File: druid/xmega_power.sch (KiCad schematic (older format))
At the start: 32 parts, among them P9 CONN_01X02, U4 XC6206P332MR

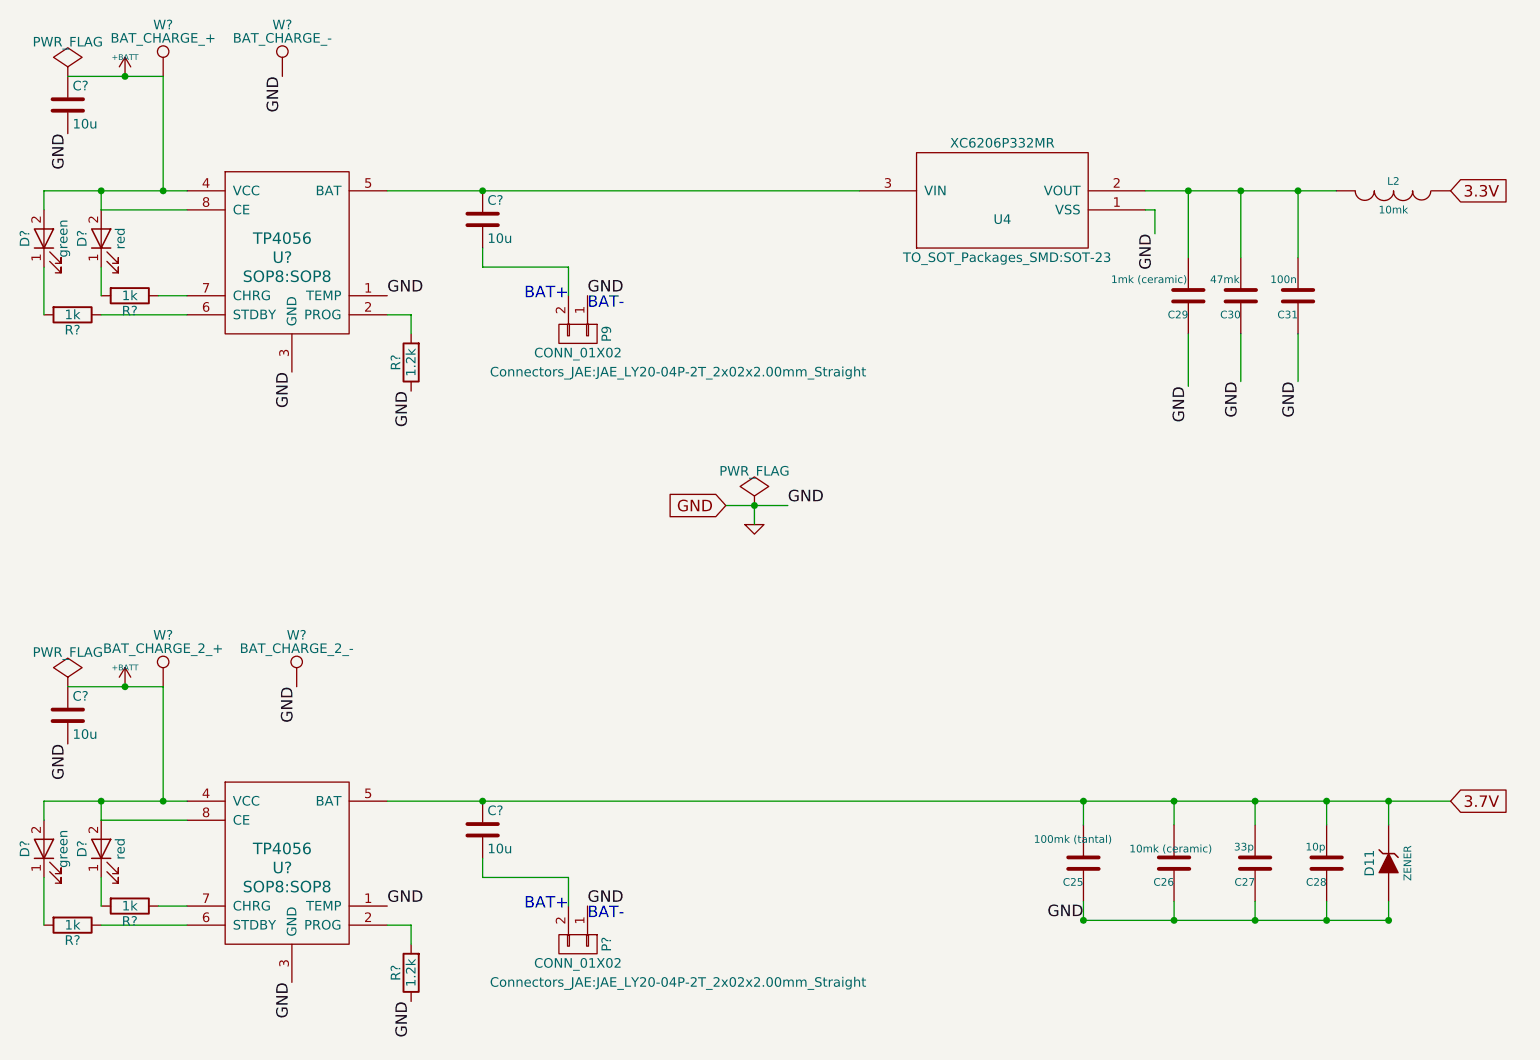
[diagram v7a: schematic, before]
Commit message: Bat connectors replaced by test points
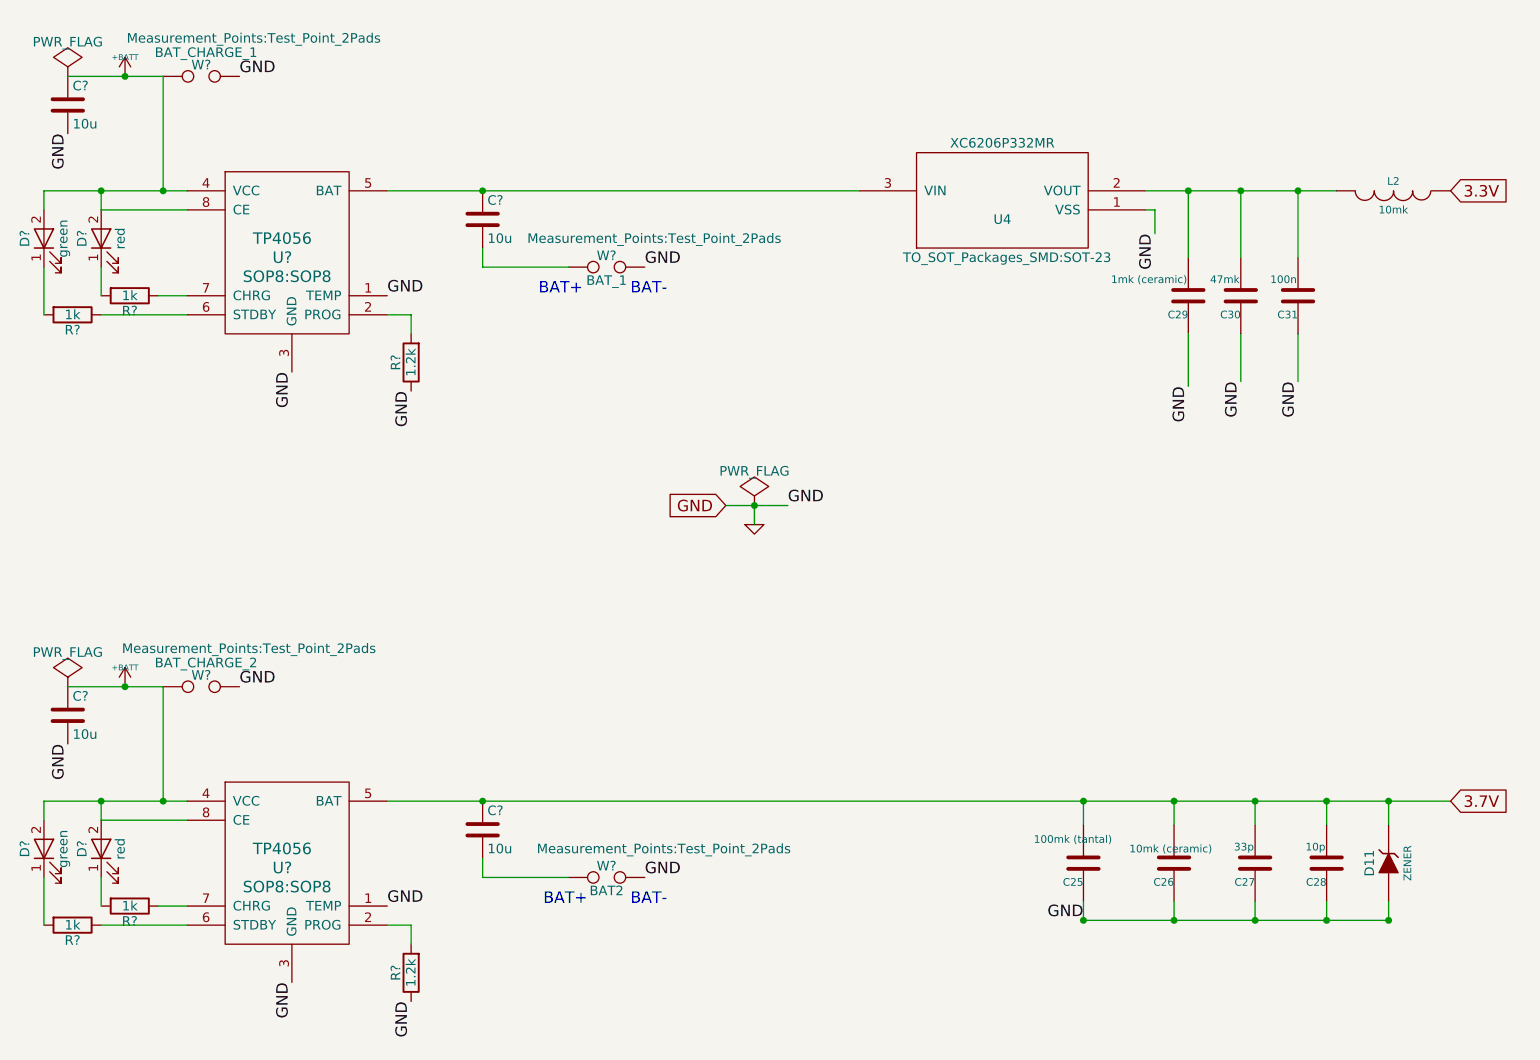
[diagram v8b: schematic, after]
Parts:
- removed P9, P?: CONN_01X02, Connectors_JAE:JAE_LY20-04P-2T_2x02x2.00mm_Straight, symbol CONN_01X02
- removed W?: BAT_CHARGE_+, symbol TEST_1P
- removed W?: BAT_CHARGE_-, symbol TEST_1P
- removed W?: BAT_CHARGE_2_+, symbol TEST_1P
- removed W?: BAT_CHARGE_2_-, symbol TEST_1P
- added W?: BAT_1, Measurement_Points:Test_Point_2Pads, symbol TEST
- added W?: BAT2, Measurement_Points:Test_Point_2Pads, symbol TEST
- added W?: BAT_CHARGE_1, Measurement_Points:Test_Point_2Pads, symbol TEST
- added W?: BAT_CHARGE_2, Measurement_Points:Test_Point_2Pads, symbol TEST
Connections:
- net +BATT: now also W?.1, W?.1
- net GND: now also W?.2, W?.2, W?.2, W?.2
- net at C?.2: now also W?.1 (x2)
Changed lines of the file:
@@
 Wire Wire Line
 	3825 2050 6300 2050
-$Comp
-L CONN_01X02 P9
-U 1 1 5AB7EB32
-P 4825 2800
-F 0 "P9" H 4825 2950 50  0000 C CNN
-F 1 "CONN_01X02" V 4925 2800 50  0000 C CNN
-F 2 "Connectors_JAE:JAE_LY20-04P-2T_2x02x2.00mm_Straight" V 5025 3325 50  0000 C CNN
-F 3 "" H 4825 2800 50  0000 C CNN
-	1    4825 2800
-	0    1    1    0
-$EndComp
 Text GLabel 5600 3700 0    60   Input ~ 0
 GND
@@
 Wire Wire Line
 	4325 2450 4775 2450
-Wire Wire Line
-	4775 2450 4775 2600
-Text Label 4875 2600 0    60   ~ 0
-GND
-Text Notes 4875 2675 0    60   ~ 0
+Text Label 5175 2450 0    60   ~ 0
+GND
+Text Notes 5100 2600 0    60   ~ 0
 BAT-
-Text Notes 4775 2625 2    60   ~ 0
+Text Notes 4850 2600 2    60   ~ 0
 BAT+\n
 $Comp
@@
 Text Label 3325 3000 3    60   ~ 0
 GND
-$Comp
-L TEST_1P W?
-U 1 1 5C6AC0DE
-P 2650 1450
-F 0 "W?" H 2650 1720 50  0000 C CNN
-F 1 "BAT_CHARGE_+" H 2650 1650 50  0000 C CNN
-F 2 "" H 2850 1450 50  0000 C CNN
-F 3 "" H 2850 1450 50  0000 C CNN
-	1    2650 1450
-	1    0    0    -1
-$EndComp
-$Comp
-L TEST_1P W?
-U 1 1 5C6AC3A7
-P 3275 1450
-F 0 "W?" H 3275 1720 50  0000 C CNN
-F 1 "BAT_CHARGE_-" H 3275 1650 50  0000 C CNN
-F 2 "" H 3475 1450 50  0000 C CNN
-F 3 "" H 3475 1450 50  0000 C CNN
-	1    3275 1450
-	1    0    0    -1
-$EndComp
-Text Label 3275 1450 3    60   ~ 0
+Text Label 3050 1450 0    60   ~ 0
 GND
 $Comp
@@
 Connection ~ 4325 5250
 $Comp
-L CONN_01X02 P?
-U 1 1 5C6B0909
-P 4825 6000
-F 0 "P?" H 4825 6150 50  0000 C CNN
-F 1 "CONN_01X02" V 4925 6000 50  0000 C CNN
-F 2 "Connectors_JAE:JAE_LY20-04P-2T_2x02x2.00mm_Straight" V 5025 6525 50  0000 C CNN
-F 3 "" H 4825 6000 50  0000 C CNN
-	1    4825 6000
-	0    1    1    0
-$EndComp
-$Comp
 L TP4056 U?
 U 1 1 5C6B090F
@@
 Wire Wire Line
 	4325 5650 4775 5650
-Wire Wire Line
-	4775 5650 4775 5800
-Text Label 4875 5800 0    60   ~ 0
-GND
-Text Notes 4875 5875 0    60   ~ 0
+Text Label 5175 5650 0    60   ~ 0
+GND
+Text Notes 5100 5800 0    60   ~ 0
 BAT-
-Text Notes 4775 5825 2    60   ~ 0
+Text Notes 4875 5800 2    60   ~ 0
 BAT+\n
 $Comp
@@
 Text Label 3325 6200 3    60   ~ 0
 GND
-$Comp
-L TEST_1P W?
-U 1 1 5C6B094E
-P 2650 4650
-F 0 "W?" H 2650 4920 50  0000 C CNN
-F 1 "BAT_CHARGE_2_+" H 2650 4850 50  0000 C CNN
-F 2 "" H 2850 4650 50  0000 C CNN
-F 3 "" H 2850 4650 50  0000 C CNN
-	1    2650 4650
-	1    0    0    -1
-$EndComp
-$Comp
-L TEST_1P W?
-U 1 1 5C6B0954
-P 3350 4650
-F 0 "W?" H 3350 4920 50  0000 C CNN
-F 1 "BAT_CHARGE_2_-" H 3350 4850 50  0000 C CNN
-F 2 "" H 3550 4650 50  0000 C CNN
-F 3 "" H 3550 4650 50  0000 C CNN
-	1    3350 4650
-	1    0    0    -1
-$EndComp
-Text Label 3350 4650 3    60   ~ 0
+Text Label 3050 4650 0    60   ~ 0
 GND
 $Comp
@@
 	1    0    0    -1
 $EndComp
+$Comp
+L TEST W?
+U 1 1 5C6B9CD1
+P 4975 2450
+F 0 "W?" H 4975 2510 50  0000 C CNN
+F 1 "BAT_1" H 4975 2380 50  0000 C CNN
+F 2 "Measurement_Points:Test_Point_2Pads" H 5225 2600 50  0000 C CNN
+F 3 "" H 4975 2450 50  0000 C CNN
+	1    4975 2450
+	1    0    0    -1
+$EndComp
+$Comp
+L TEST W?
+U 1 1 5C6BA4AE
+P 4975 5650
+F 0 "W?" H 4975 5710 50  0000 C CNN
+F 1 "BAT2" H 4975 5580 50  0000 C CNN
+F 2 "Measurement_Points:Test_Point_2Pads" H 5275 5800 50  0000 C CNN
+F 3 "" H 4975 5650 50  0000 C CNN
+	1    4975 5650
+	1    0    0    -1
+$EndComp
+$Comp
+L TEST W?
+U 1 1 5C6BB1A8
+P 2850 1450
+F 0 "W?" H 2850 1510 50  0000 C CNN
+F 1 "BAT_CHARGE_1" H 2875 1575 50  0000 C CNN
+F 2 "Measurement_Points:Test_Point_2Pads" H 3125 1650 50  0000 C CNN
+F 3 "" H 2850 1450 50  0000 C CNN
+	1    2850 1450
+	1    0    0    -1
+$EndComp
+$Comp
+L TEST W?
+U 1 1 5C6BB612
+P 2850 4650
+F 0 "W?" H 2850 4710 50  0000 C CNN
+F 1 "BAT_CHARGE_2" H 2875 4775 50  0000 C CNN
+F 2 "Measurement_Points:Test_Point_2Pads" H 3100 4850 50  0000 C CNN
+F 3 "" H 2850 4650 50  0000 C CNN
+	1    2850 4650
+	1    0    0    -1
+$EndComp
